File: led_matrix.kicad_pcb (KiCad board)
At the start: 2 copper layers, 85.1 x 109.2 mm, 116 parts, among them J1 I2C, J2 Extra, J3 Address, J4 +5V, J5 GND, J6 Power Input, J7 Columns, J8 Row Addr., Q1 2N3904, Q2 2N3904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

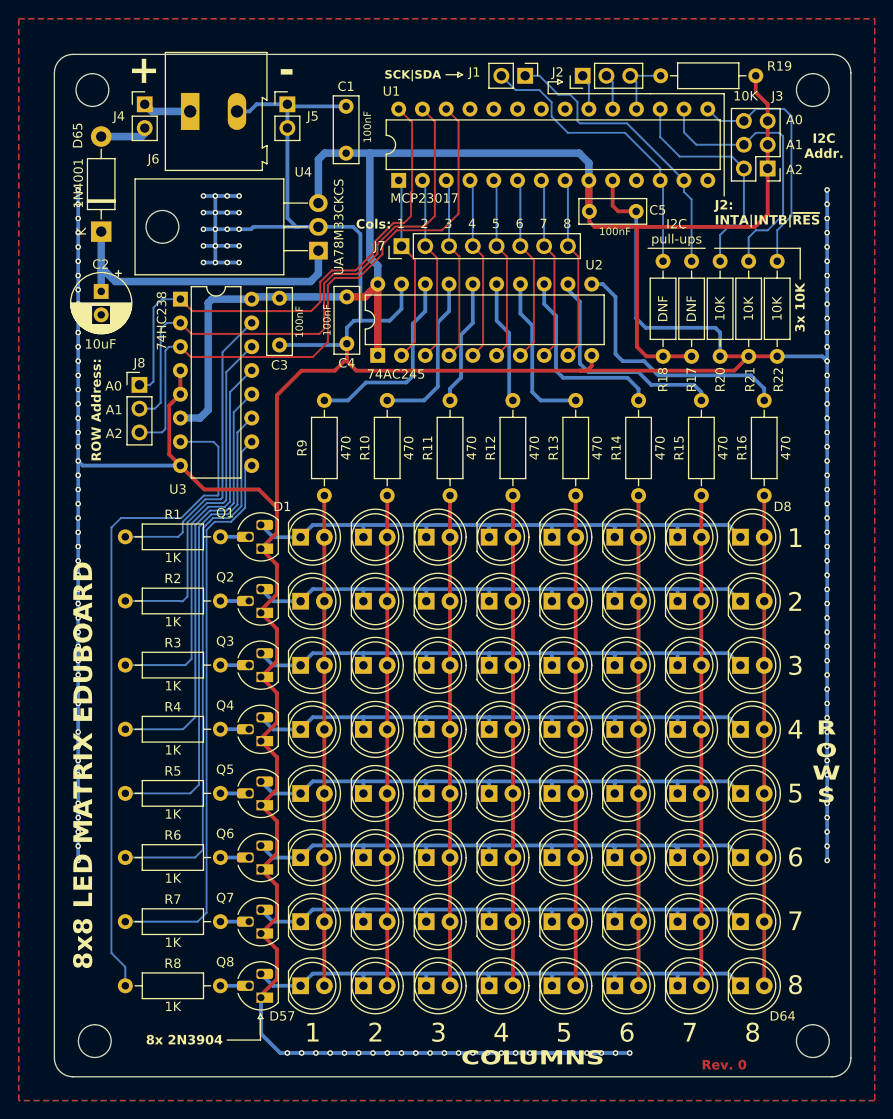
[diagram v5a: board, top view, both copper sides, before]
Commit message: Reorganized some traces
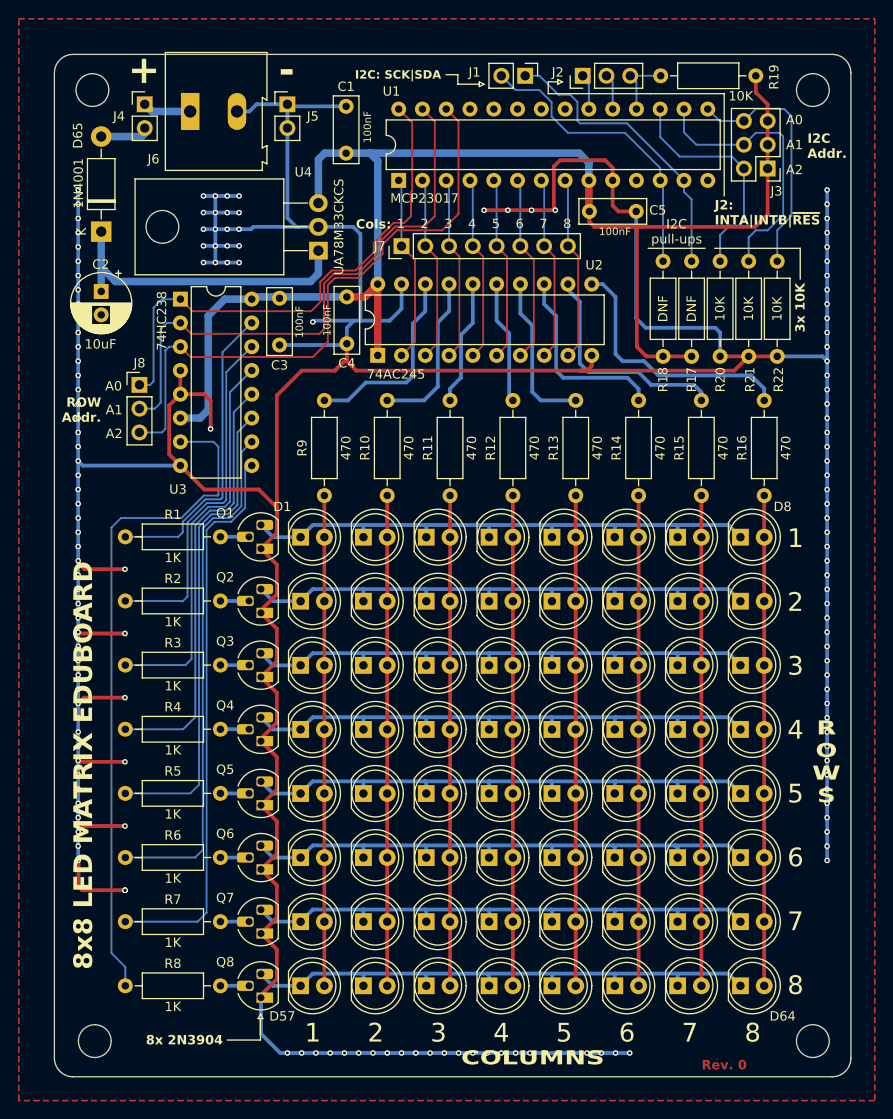
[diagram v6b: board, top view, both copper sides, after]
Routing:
- net GND: track 488.4 -> 554.1 mm, vias 141 -> 154
- net VCC: track 150.5 -> 149.7 mm
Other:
- board text added: "I2C: SCK|SDA"
- board text added: "ROW Addr."
- board text removed: "ROW Address:"
- board text removed: "SCK|SDA"

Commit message: Update the gerbers for this board, reorganized some text
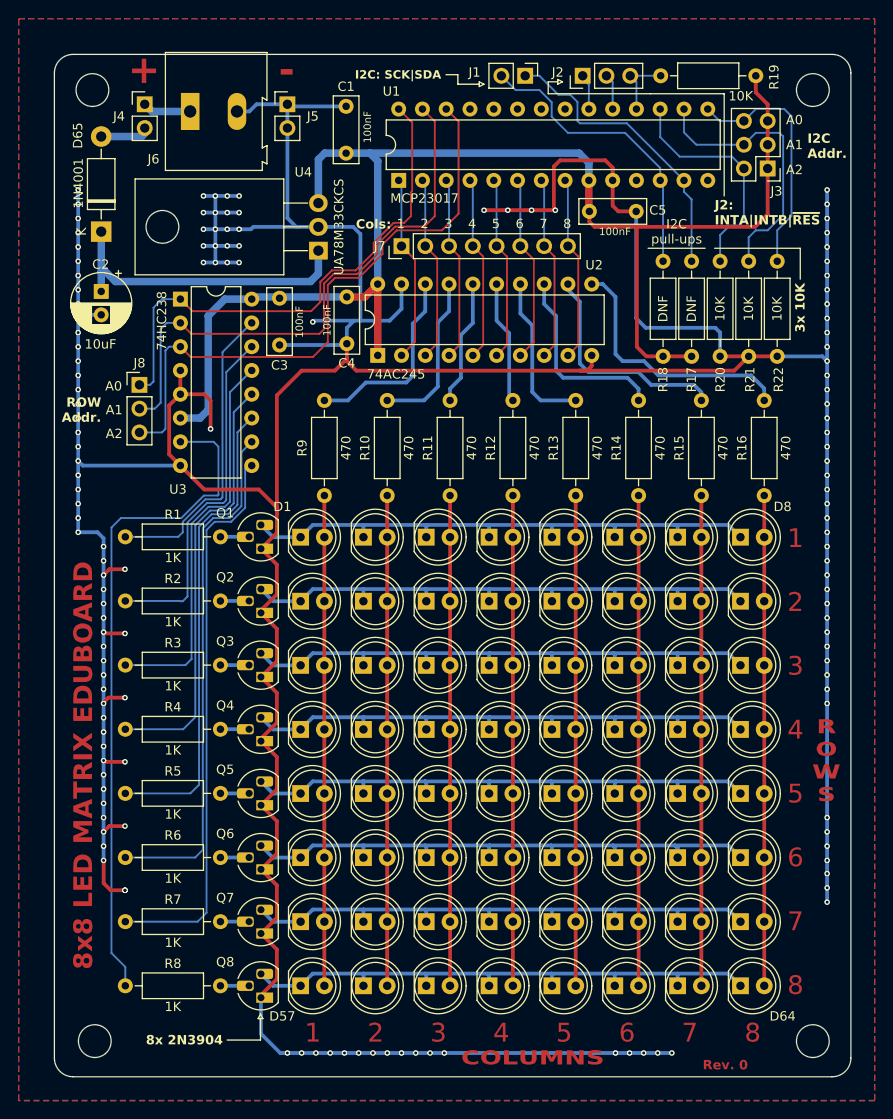
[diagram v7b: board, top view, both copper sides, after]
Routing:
- net GND: track 554.1 -> 551.3 mm, vias 154 -> 142

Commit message: Fix missing 5V connection between two points of an header
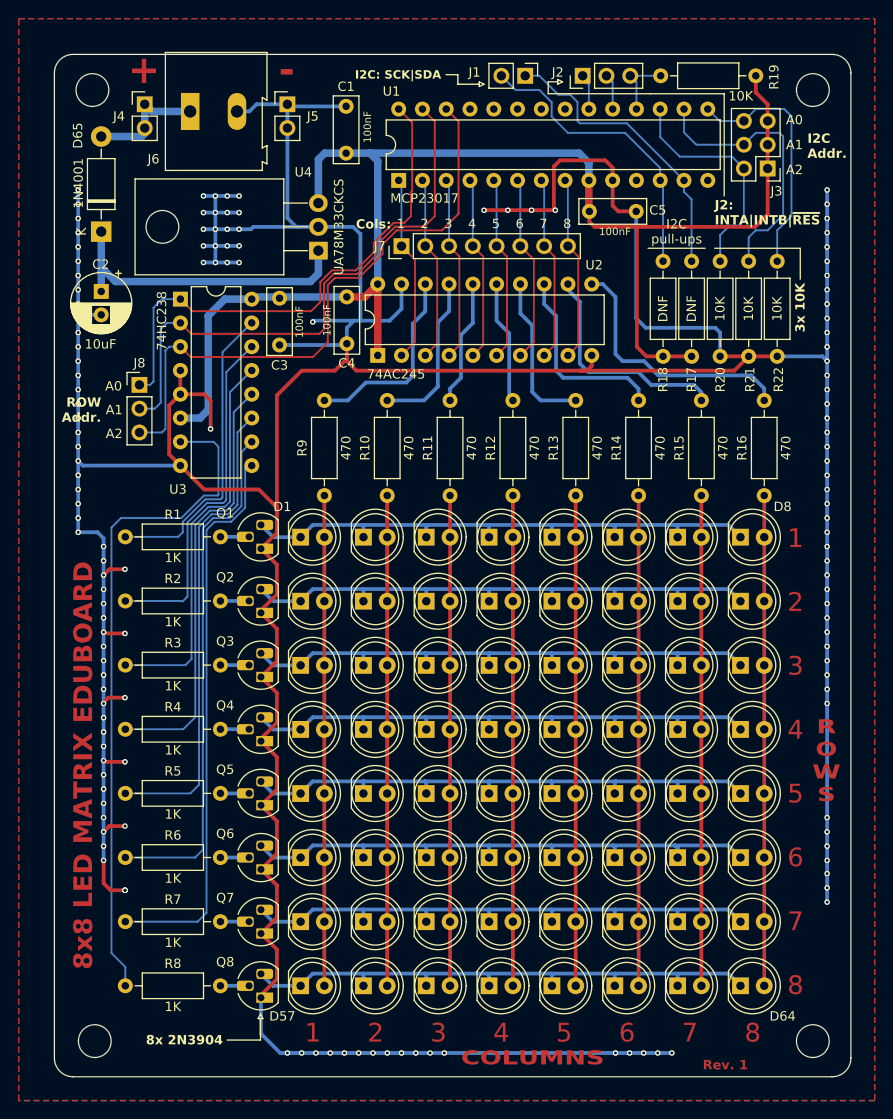
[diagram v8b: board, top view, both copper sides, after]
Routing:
- net +5V: track 10.5 -> 13.1 mm
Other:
- board text added: "Rev. 1"
- board text removed: "Rev. 0"
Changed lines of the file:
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@@
 		)
 	)
-	(gr_text "Rev. 0"
+	(gr_text "Rev. 1"
 		(at 171.831 151.003 0)
 		(layer "F.Cu")
@@
 		)
 	)
-	(gr_text "Rev. 0"
+	(gr_text "Rev. 1"
 		(at 171.831 151.003 0)
 		(layer "F.Mask")
@@
 		(width 0.8)
 		(layer "B.Cu")
+		(net 19)
+	)
+	(segment
+		(start 109.805572 50.910714)
+		(end 109.805572 48.370714)
+		(width 0.8)
+		(layer "B.Cu")
